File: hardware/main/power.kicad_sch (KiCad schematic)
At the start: 31 parts, among them Q1 SSM3J338R

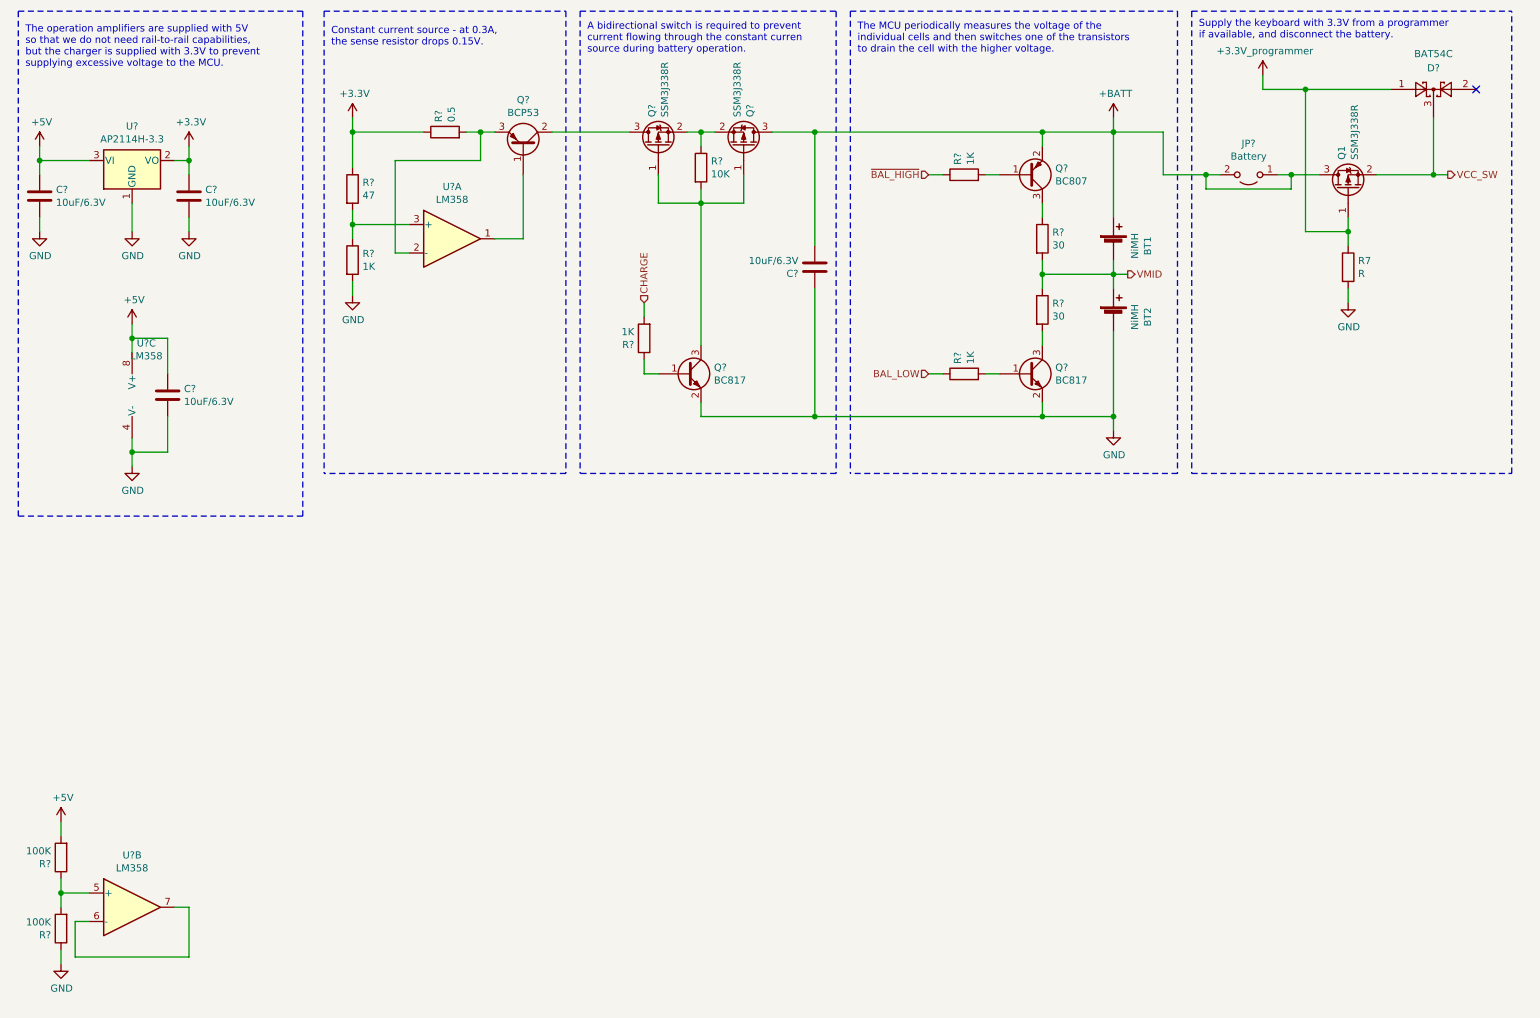
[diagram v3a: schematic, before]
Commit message: Fix power supply footprints and set references.
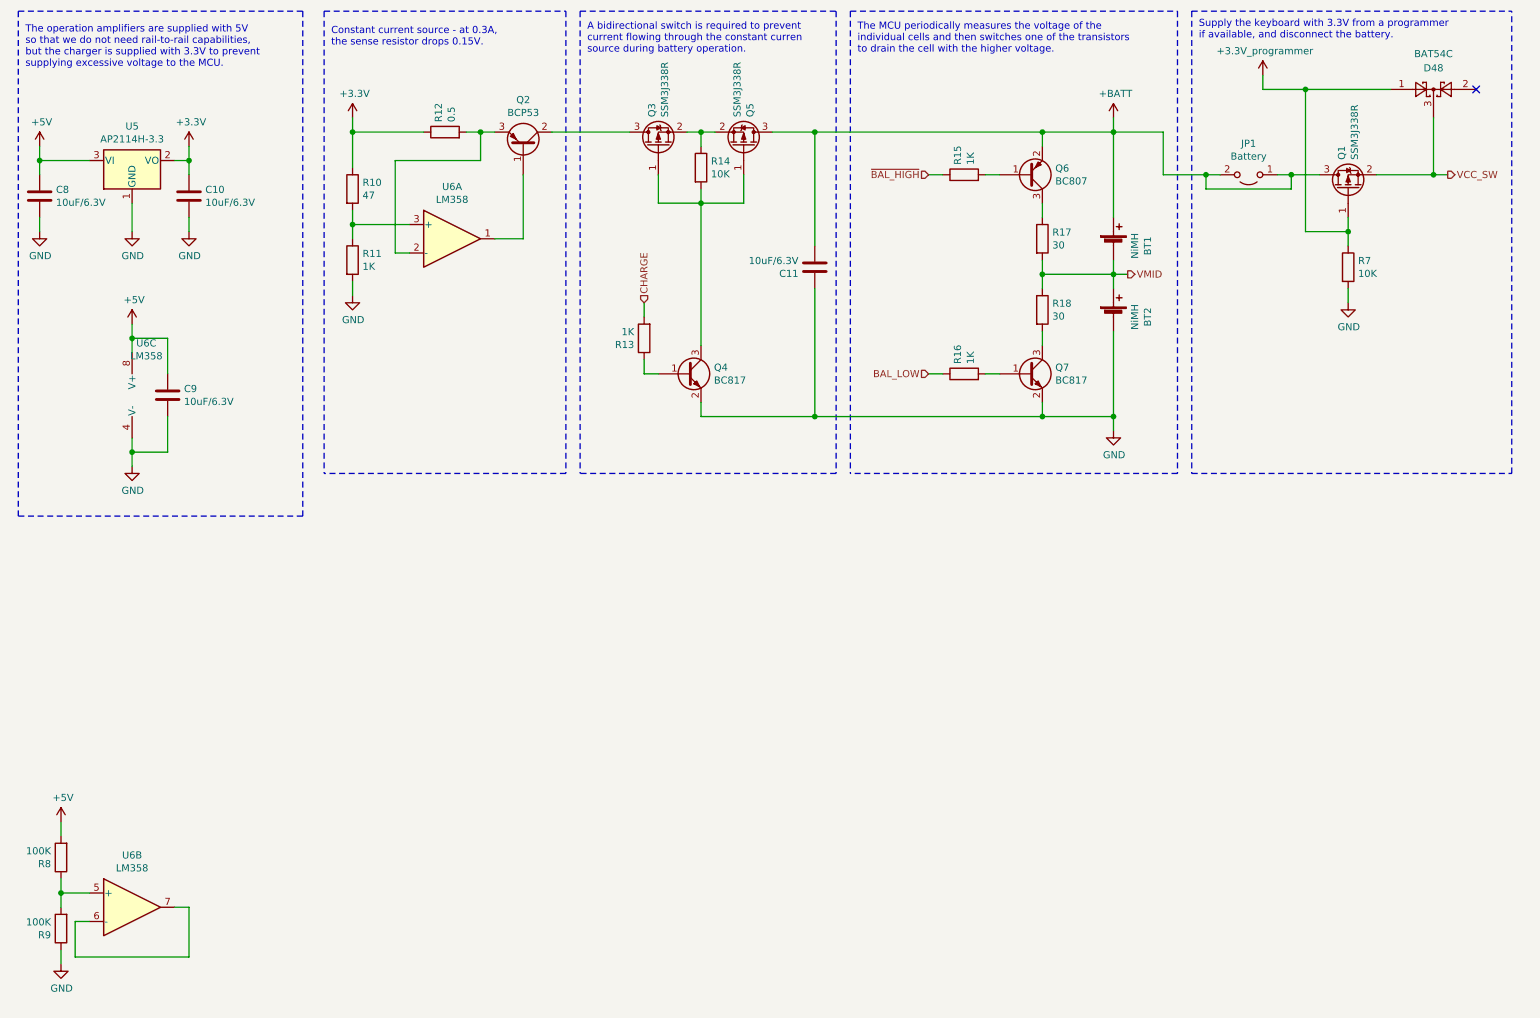
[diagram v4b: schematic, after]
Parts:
- BT1, BT2: footprint (none) -> Connector_PinHeader_2.54mm:PinHeader_1x02_P2.54mm_Horizontal
- C10, C11, C8, C9: renamed from C?; footprint (none) -> Capacitor_SMD:C_0805_2012Metric
- JP1: renamed from JP?; footprint (none) -> Connector_PinHeader_2.54mm:PinHeader_1x02_P2.54mm_Horizontal
- Q2: renamed from Q?; footprint Package_TO_SOT_SMD:SOT-223-3_TabPin2 -> Package_TO_SOT_SMD:SOT-223
- R12: renamed from R?; footprint (none) -> Resistor_SMD:R_1206_3216Metric; Mouser (none) -> 588-KDV12FR510ET; Part Name (none) -> Ohmite KDV12FR510ET
- R7: value R -> 10K; footprint (none) -> Resistor_SMD:R_0603_1608Metric
- gave numbers to parts that had none: 18

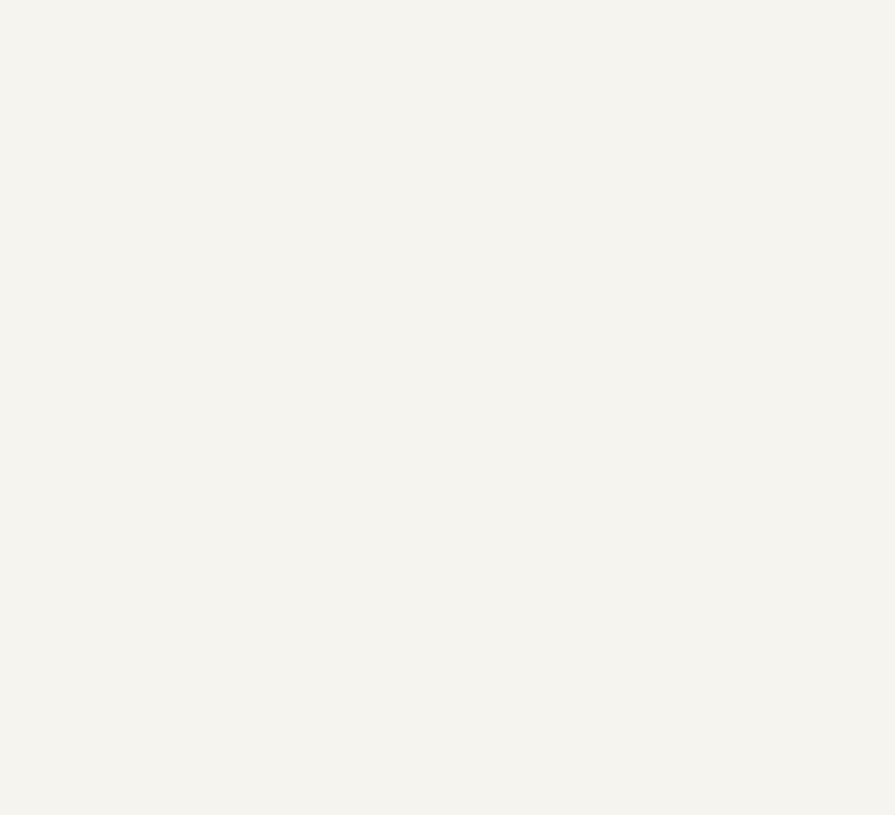
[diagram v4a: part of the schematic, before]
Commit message: Add signal to tell the MCU that USB is connected.
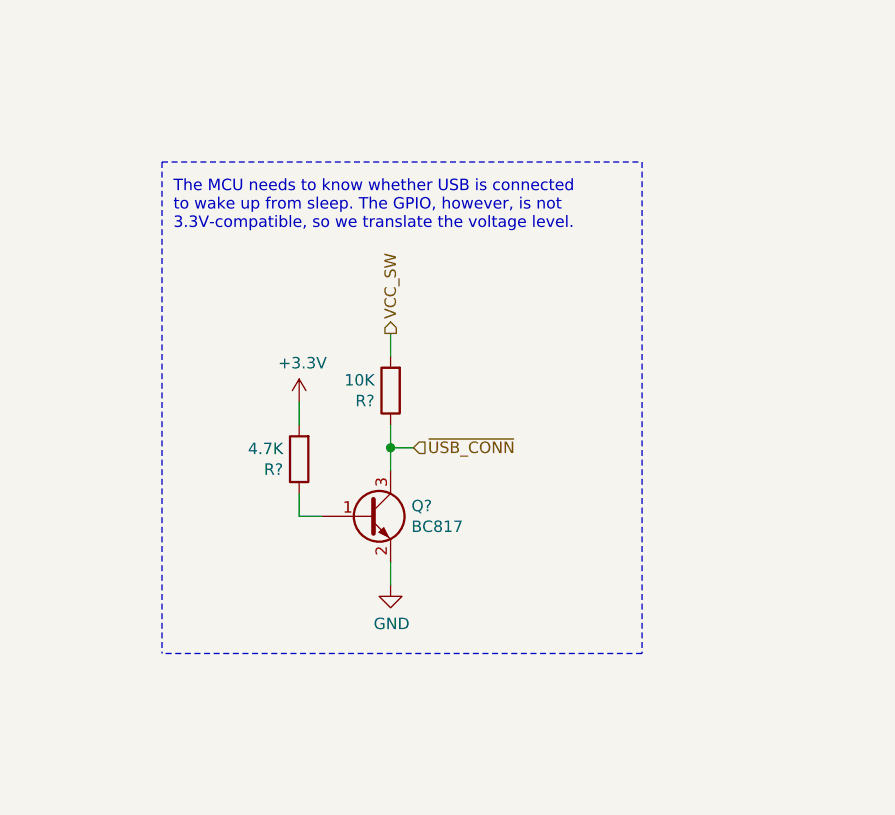
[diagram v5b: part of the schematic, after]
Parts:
- added Q?: BC817, Package_TO_SOT_SMD:SOT-23, symbol Transistor_BJT:BC817
- added R?: 10K, Resistor_SMD:R_0603_1608Metric, symbol Device:R
- added R?: 4.7K, Resistor_SMD:R_0603_1608Metric, symbol Device:R
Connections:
- net +3V3: now also R?.2
- net GND: now also Q?.2 (E)
- net VCC_SW: now also R?.2
- new net: Q?.1 (B), R?.1
- new net ~USB_CONN: Q?.3 (C), R?.1
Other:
- note added: "The MCU needs to know whether USB is connected to wake up from sleep. The GPIO, however, is not 3.3V-compatible, so we translate the voltage level."
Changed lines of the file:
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@@
   (junction (at 74.93 55.88) (diameter 1.016) (color 0 0 0 0))
   (junction (at 97.79 39.37) (diameter 1.016) (color 0 0 0 0))
+  (junction (at 120.65 153.67) (diameter 1.016) (color 0 0 0 0))
   (junction (at 137.16 39.37) (diameter 1.016) (color 0 0 0 0))
   (junction (at 137.16 52.07) (diameter 1.016) (color 0 0 0 0))
@@
     (stroke (width 0) (type solid) (color 0 0 0 0))
   )
+  (wire (pts (xy 110.49 148.59) (xy 110.49 151.13))
+    (stroke (width 0) (type solid) (color 0 0 0 0))
+  )
+  (wire (pts (xy 110.49 158.75) (xy 110.49 161.29))
+    (stroke (width 0) (type solid) (color 0 0 0 0))
+  )
+  (wire (pts (xy 110.49 161.29) (xy 113.03 161.29))
+    (stroke (width 0) (type solid) (color 0 0 0 0))
+  )
+  (wire (pts (xy 120.65 140.97) (xy 120.65 143.51))
+    (stroke (width 0) (type solid) (color 0 0 0 0))
+  )
+  (wire (pts (xy 120.65 151.13) (xy 120.65 153.67))
+    (stroke (width 0) (type solid) (color 0 0 0 0))
+  )
+  (wire (pts (xy 120.65 153.67) (xy 120.65 156.21))
+    (stroke (width 0) (type solid) (color 0 0 0 0))
+  )
+  (wire (pts (xy 120.65 153.67) (xy 123.19 153.67))
+    (stroke (width 0) (type solid) (color 0 0 0 0))
+  )
+  (wire (pts (xy 120.65 166.37) (xy 120.65 168.91))
+    (stroke (width 0) (type solid) (color 0 0 0 0))
+  )
   (wire (pts (xy 127 69.85) (xy 127 72.39))
     (stroke (width 0) (type solid) (color 0 0 0 0))
@@
     (stroke (width 0) (type dash) (color 0 0 0 0))
   )
+  (polyline (pts (xy 95.25 121.92) (xy 95.25 176.53))
+    (stroke (width 0) (type dash) (color 0 0 0 0))
+  )
+  (polyline (pts (xy 95.25 121.92) (xy 148.59 121.92))
+    (stroke (width 0) (type dash) (color 0 0 0 0))
+  )
   (polyline (pts (xy 113.03 17.78) (xy 113.03 100.33))
     (stroke (width 0) (type dash) (color 0 0 0 0))
@@
   )
   (polyline (pts (xy 115.57 17.78) (xy 161.29 17.78))
+    (stroke (width 0) (type dash) (color 0 0 0 0))
+  )
+  (polyline (pts (xy 148.59 121.92) (xy 148.59 176.53))
+    (stroke (width 0) (type dash) (color 0 0 0 0))
+  )
+  (polyline (pts (xy 148.59 176.53) (xy 95.25 176.53))
     (stroke (width 0) (type dash) (color 0 0 0 0))
   )
@@
     (effects (font (size 1.27 1.27)) (justify left bottom))
   )
+  (text "The MCU needs to know whether USB is connected\nto wake up from sleep. The GPIO, however, is not\n3.3V-compatible, so we translate the voltage level."
+    (at 96.52 129.54 0)
+    (effects (font (size 1.27 1.27)) (justify left bottom))
+  )
   (text "A bidirectional switch is required to prevent\ncurrent flowing through the constant curren\nsource during battery operation."
     (at 116.84 25.4 0)
@@
     (effects (font (size 1.27 1.27)) (justify left bottom))
   )
+  (hierarchical_label "VCC_SW" (shape output) (at 120.65 140.97 90)
+    (effects (font (size 1.27 1.27)) (justify left))
+  )
+  (hierarchical_label "~USB_CONN" (shape input) (at 123.19 153.67 0)
+    (effects (font (size 1.27 1.27)) (justify left))
+  )
   (hierarchical_label "CHARGE" (shape input) (at 127 69.85 90)
     (effects (font (size 1.27 1.27)) (justify left))
@@
     )
   )
+  (symbol (lib_id "power:+3.3V") (at 110.49 148.59 0) (unit 1)
+    (in_bom yes) (on_board yes)
+    (property "Reference" "#PWR?" (id 0) (at 110.49 152.4 0)
+      (effects (font (size 1.27 1.27)) hide)
+    )
+    (property "Value" "+3.3V" (id 1) (at 110.8583 144.2656 0))
+    (property "Footprint" "" (id 2) (at 110.49 148.59 0)
+      (effects (font (size 1.27 1.27)) hide)
+    )
+    (property "Datasheet" "" (id 3) (at 110.49 148.59 0)
+      (effects (font (size 1.27 1.27)) hide)
+    )
+  )
   (symbol (lib_id "power:+BATT") (at 210.82 36.83 0) (unit 1)
     (in_bom yes) (on_board yes)
@@
     )
   )
+  (symbol (lib_id "power:GND") (at 120.65 168.91 0) (unit 1)
+    (in_bom yes) (on_board yes)
+    (property "Reference" "#PWR?" (id 0) (at 120.65 175.26 0)
+      (effects (font (size 1.27 1.27)) hide)
+    )
+    (property "Value" "GND" (id 1) (at 120.7643 173.2344 0))
+    (property "Footprint" "" (id 2) (at 120.65 168.91 0)
+      (effects (font (size 1.27 1.27)) hide)
+    )
+    (property "Datasheet" "" (id 3) (at 120.65 168.91 0)
+      (effects (font (size 1.27 1.27)) hide)
+    )
+  )
   (symbol (lib_id "power:GND") (at 210.82 92.71 0) (unit 1)
     (in_bom yes) (on_board yes)
@@
     )
     (property "Mouser" "588-KDV12FR510ET" (id 5) (at 91.44 39.37 0)
+      (effects (font (size 1.27 1.27)) hide)
+    )
+  )
+  (symbol (lib_id "Device:R") (at 110.49 154.94 180) (unit 1)
+    (in_bom yes) (on_board yes)
+    (property "Reference" "R?" (id 0) (at 108.7119 156.0894 0)
+      (effects (font (size 1.27 1.27)) (justify left))
+    )
+    (property "Value" "4.7K" (id 1) (at 108.712 153.791 0)
+      (effects (font (size 1.27 1.27)) (justify left))
+    )
+    (property "Footprint" "Resistor_SMD:R_0603_1608Metric" (id 2) (at 112.268 154.94 90)
+      (effects (font (size 1.27 1.27)) hide)
+    )
+    (property "Datasheet" "~" (id 3) (at 110.49 154.94 0)
+      (effects (font (size 1.27 1.27)) hide)
+    )
+  )
+  (symbol (lib_id "Device:R") (at 120.65 147.32 180) (unit 1)
+    (in_bom yes) (on_board yes)
+    (property "Reference" "R?" (id 0) (at 118.8719 148.4694 0)
+      (effects (font (size 1.27 1.27)) (justify left))
+    )
+    (property "Value" "10K" (id 1) (at 118.872 146.171 0)
+      (effects (font (size 1.27 1.27)) (justify left))
+    )
+    (property "Footprint" "Resistor_SMD:R_0603_1608Metric" (id 2) (at 122.428 147.32 90)
+      (effects (font (size 1.27 1.27)) hide)
+    )
+    (property "Datasheet" "~" (id 3) (at 120.65 147.32 0)
       (effects (font (size 1.27 1.27)) hide)
     )
@@
     )
   )
+  (symbol (lib_id "Transistor_BJT:BC817") (at 118.11 161.29 0) (unit 1)
+    (in_bom yes) (on_board yes)
+    (property "Reference" "Q?" (id 0) (at 122.9615 160.1406 0)
+      (effects (font (size 1.27 1.27)) (justify left))
+    )
+    (property "Value" "BC817" (id 1) (at 122.9615 162.4393 0)
+      (effects (font (size 1.27 1.27)) (justify left))
+    )
+    (property "Footprint" "Package_TO_SOT_SMD:SOT-23" (id 2) (at 123.19 163.195 0)
+      (effects (font (size 1.27 1.27) italic) (justify left) hide)
+    )
+    (property "Datasheet" "https://www.onsemi.com/pub/Collateral/BC818-D.pdf" (id 3) (at 118.11 161.29 0)
+      (effects (font (size 1.27 1.27)) (justify left) hide)
+    )
+  )
